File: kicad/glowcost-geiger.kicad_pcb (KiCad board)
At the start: 2 copper layers, 120 x 40 mm, 77 parts, among them J1 JST GH 4-pin, J2 C142864 DNP, J3 C142864 DNP, Q1 MMBT3904LT1G, Q2 MMBT3904LT1G

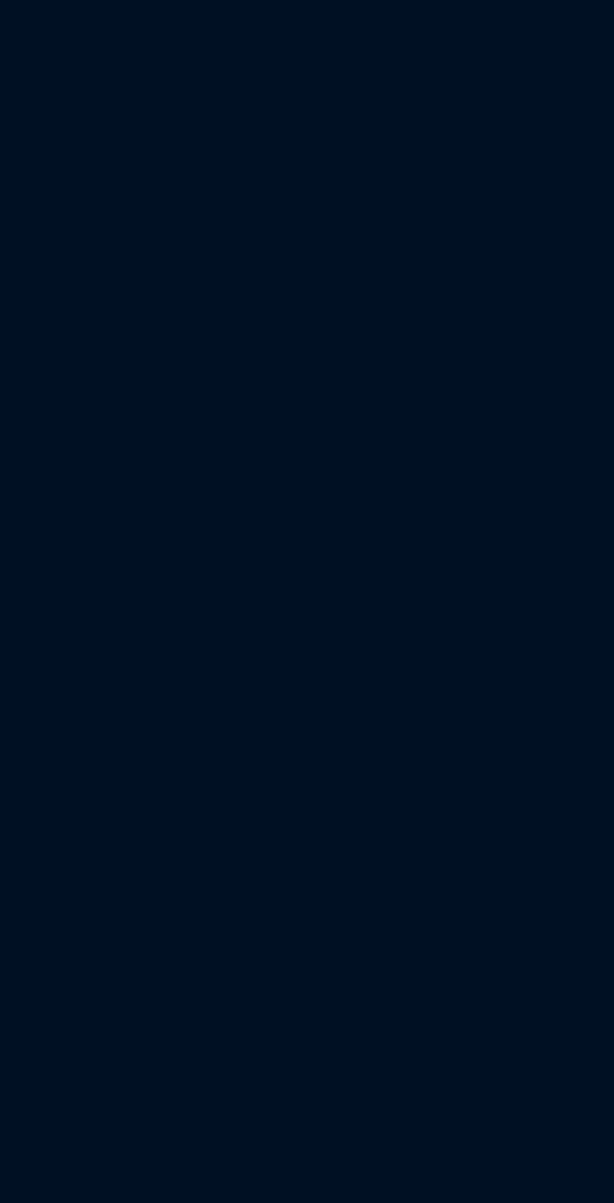
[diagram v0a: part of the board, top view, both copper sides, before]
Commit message: Clean KiCad sheet and place implementation parts
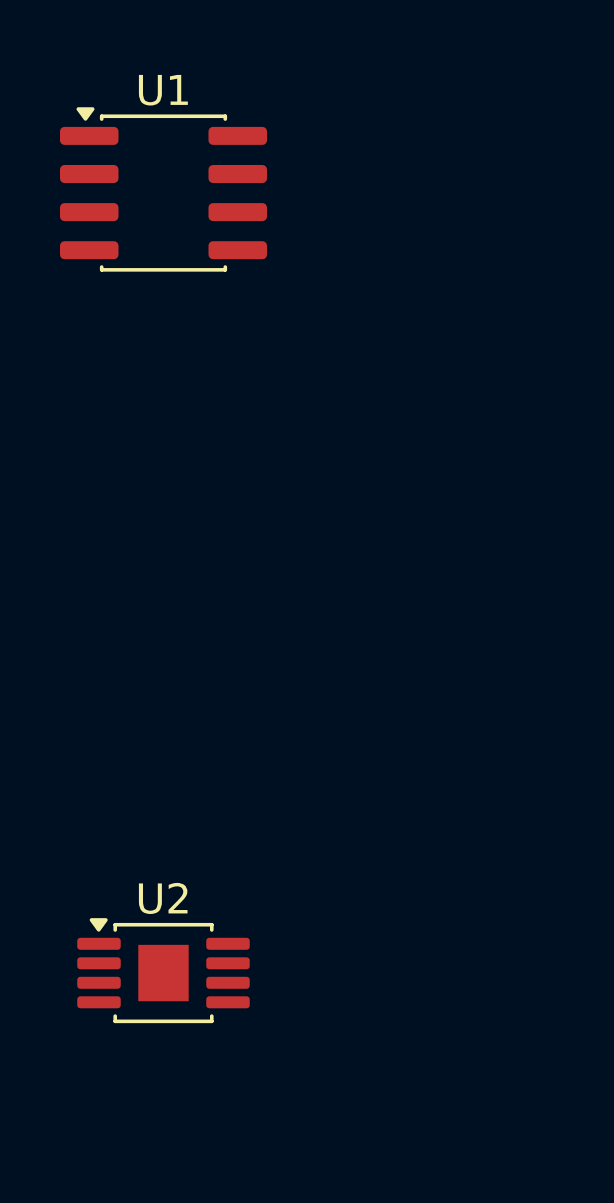
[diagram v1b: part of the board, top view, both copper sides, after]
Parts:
- added U1: TLC555IDR, U1, F.Cu at (-24.0, -13.0)
- added U2: MCP6562T-E/MS, U2, F.Cu at (-24.0, 13.0)

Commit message: Apply end connector placement and 0.8mm stackup
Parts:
- moved J1 54.1 mm to (4.50, 100.0), turned to 90 degrees
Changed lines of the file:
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@@
 	(generator_version "10.0")
 	(general
-		(thickness 1.6)
+		(thickness 0.8)
 		(legacy_teardrops no)
 	)
@@
 	(footprint "glowcost:J1"
 		(layer "F.Cu")
-		(at 57 113)
+		(at 4.5 100 90)
 		(property "Reference" "J1"
-			(at 0 -3 0)
+			(at 0 -3 90)
 			(layer "F.SilkS")
 			(hide yes)
@@
 		)
 		(property "Value" "JST GH 4-pin"
-			(at 0 3 0)
+			(at 0 3 90)
 			(layer "F.Fab")
 			(hide yes)
@@
 		)
 		(property "Datasheet" ""
-			(at 0 0 0)
+			(at 0 0 90)
 			(layer "F.Fab")
 			(hide yes)
@@
 		)
 		(property "Description" ""
-			(at 0 0 0)
+			(at 0 0 90)
 			(layer "F.Fab")
 			(hide yes)
@@
 		)
 		(property "Supplier Part Number" "C161692"
-			(at 0 0 0)
+			(at 0 0 90)
 			(layer "F.Fab")
 			(hide yes)
@@
 		)
 		(property "MPN" "BM04B-GHS-TBT(LF)(SN)"
-			(at 0 0 0)
+			(at 0 0 90)
 			(layer "F.Fab")
 			(hide yes)
@@
 		)
 		(property "LCSC" "C161692"
-			(at 0 0 0)
+			(at 0 0 90)
 			(layer "F.Fab")
 			(hide yes)
@@
 		)
 		(pad "" smd rect
-			(at -3.725 -1.4)
+			(at -3.725 -1.4 90)
 			(size 1 2.8)
 			(layers "F.Cu" "F.Mask" "F.Paste")
 		)
 		(pad "" smd rect
-			(at 3.725 -1.4)
+			(at 3.725 -1.4 90)
 			(size 1 2.8)
 			(layers "F.Cu" "F.Mask" "F.Paste")
 		)
 		(pad "1" smd rect
-			(at -1.875 1.95)
+			(at -1.875 1.95 90)
 			(size 0.6 1.7)
 			(layers "F.Cu" "F.Mask" "F.Paste")
@@
 		)
 		(pad "2" smd rect
-			(at -0.625 1.95)
+			(at -0.625 1.95 90)
 			(size 0.6 1.7)
 			(layers "F.Cu" "F.Mask" "F.Paste")
@@
 		)
 		(pad "3" smd rect
-			(at 0.625 1.95)
+			(at 0.625 1.95 90)
 			(size 0.6 1.7)
 			(layers "F.Cu" "F.Mask" "F.Paste")
@@
 		)
 		(pad "4" smd rect
-			(at 1.875 1.95)
+			(at 1.875 1.95 90)
 			(size 0.6 1.7)
 			(layers "F.Cu" "F.Mask" "F.Paste")

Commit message: Center Pi connector on left tube end
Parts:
- moved J1 40.0 mm to (44.5, 100.0)
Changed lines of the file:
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@@
 	(footprint "glowcost:J1"
 		(layer "F.Cu")
-		(at 4.5 100 90)
+		(at 44.5 100 90)
 		(property "Reference" "J1"
 			(at 0 -3 90)

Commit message: Rebuild sheet metal clip and narrow PCB outline
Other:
- board size 120 x 40 mm -> 120 x 32 mm
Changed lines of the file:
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@@
 	(generator_version "10.0")
 	(general
-		(thickness 0.8)
+		(thickness 1.6)
 		(legacy_teardrops no)
 	)
@@
 	)
 	(gr_line
-		(start 40 82)
-		(end 40 118)
+		(start 40 86)
+		(end 40 114)
 		(stroke
 			(width 0.1)
@@
 	)
 	(gr_line
-		(start 40 118)
-		(end 42 120)
+		(start 40 114)
+		(end 42 116)
 		(stroke
 			(width 0.1)
@@
 	)
 	(gr_line
-		(start 42 80)
-		(end 40 82)
+		(start 42 84)
+		(end 40 86)
 		(stroke
 			(width 0.1)
@@
 	)
 	(gr_line
-		(start 42 120)
-		(end 158 120)
+		(start 42 116)
+		(end 158 116)
 		(stroke
 			(width 0.1)
@@
 	)
 	(gr_line
-		(start 158 80)
-		(end 42 80)
+		(start 158 84)
+		(end 42 84)
 		(stroke
 			(width 0.1)
@@
 	)
 	(gr_line
-		(start 158 120)
-		(end 160 118)
+		(start 158 116)
+		(end 160 114)
 		(stroke
 			(width 0.1)
@@
 	)
 	(gr_line
-		(start 160 82)
-		(end 158 80)
+		(start 160 86)
+		(end 158 84)
 		(stroke
 			(width 0.1)
@@
 	)
 	(gr_line
-		(start 160 118)
-		(end 160 82)
+		(start 160 114)
+		(end 160 86)
 		(stroke
 			(width 0.1)

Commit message: Add HV isolation slots and clean assembly notes
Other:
- outline, holes or cut-outs redrawn
- board text added: "HV SERVICE - DISCHARGE BEFORE TOUCH"
- board text added: "HV SLOT 1mm"
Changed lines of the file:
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@@
 		(layer "Edge.Cuts")
+	)
+	(gr_rect
+		(start 74 87)
+		(end 75 113)
+		(stroke (width 0.05) (type default))
+		(fill none)
+		(layer "Edge.Cuts")
+	)
+	(gr_rect
+		(start 86 87)
+		(end 87 113)
+		(stroke (width 0.05) (type default))
+		(fill none)
+		(layer "Edge.Cuts")
+	)
+	(gr_text "HV SLOT 1mm"
+		(at 80 85.7)
+		(layer "F.SilkS")
+		(effects (font (size 0.8 0.8) (thickness 0.12)))
+	)
+	(gr_text "HV SERVICE - DISCHARGE BEFORE TOUCH"
+		(at 80 114.3)
+		(layer "F.SilkS")
+		(effects (font (size 0.8 0.8) (thickness 0.12)))
 	)
 	(gr_text "TP1 V3V3"
